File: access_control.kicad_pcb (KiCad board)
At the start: 2 copper layers, 72 parts, among them J1 Conn_01x04_Pin, J10 Screw_Terminal_01x02, J2 Screw_Terminal_01x04, J3 Screw_Terminal_01x04, J4 Screw_Terminal_01x02, J5 Screw_Terminal_01x04, J6 Screw_Terminal_01x04, J7 Screw_Terminal_01x02, J8 Screw_Terminal_01x02, J9 Screw_Terminal_01x02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

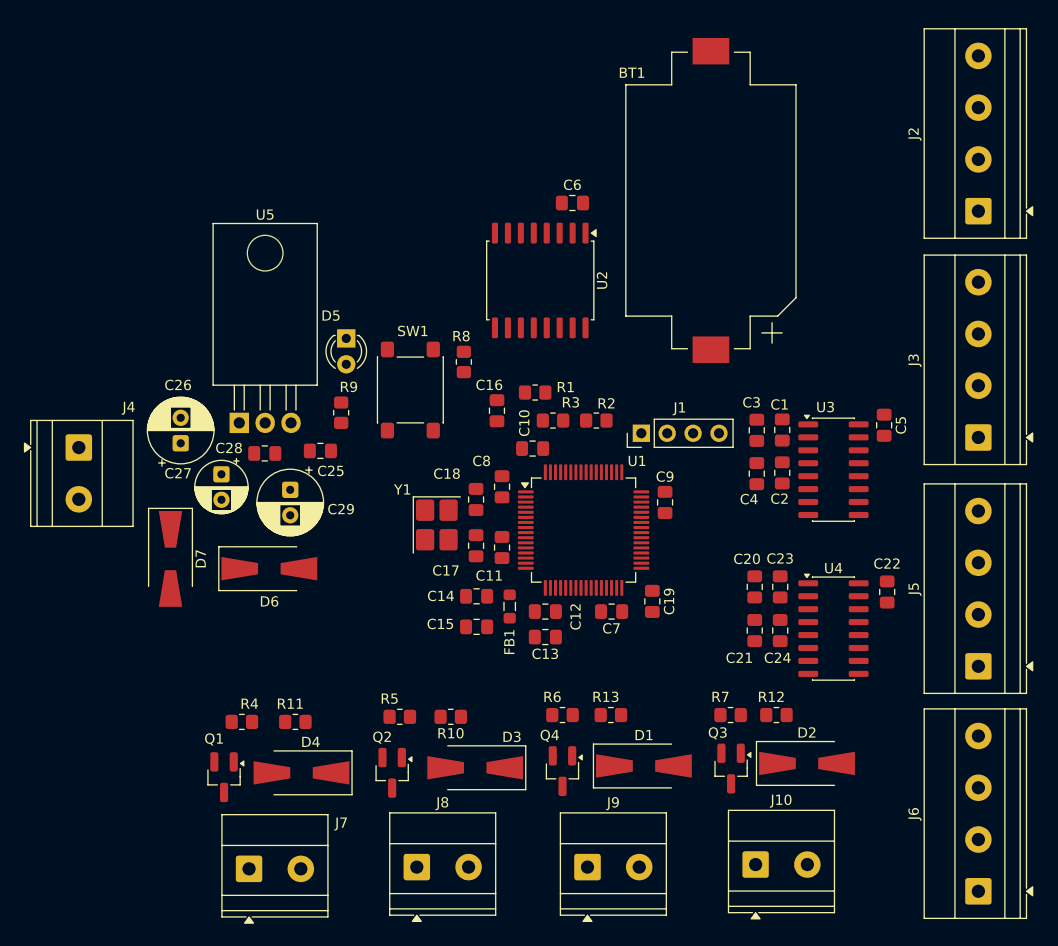
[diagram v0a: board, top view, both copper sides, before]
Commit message: Finished the PCB routing and placement of the components.
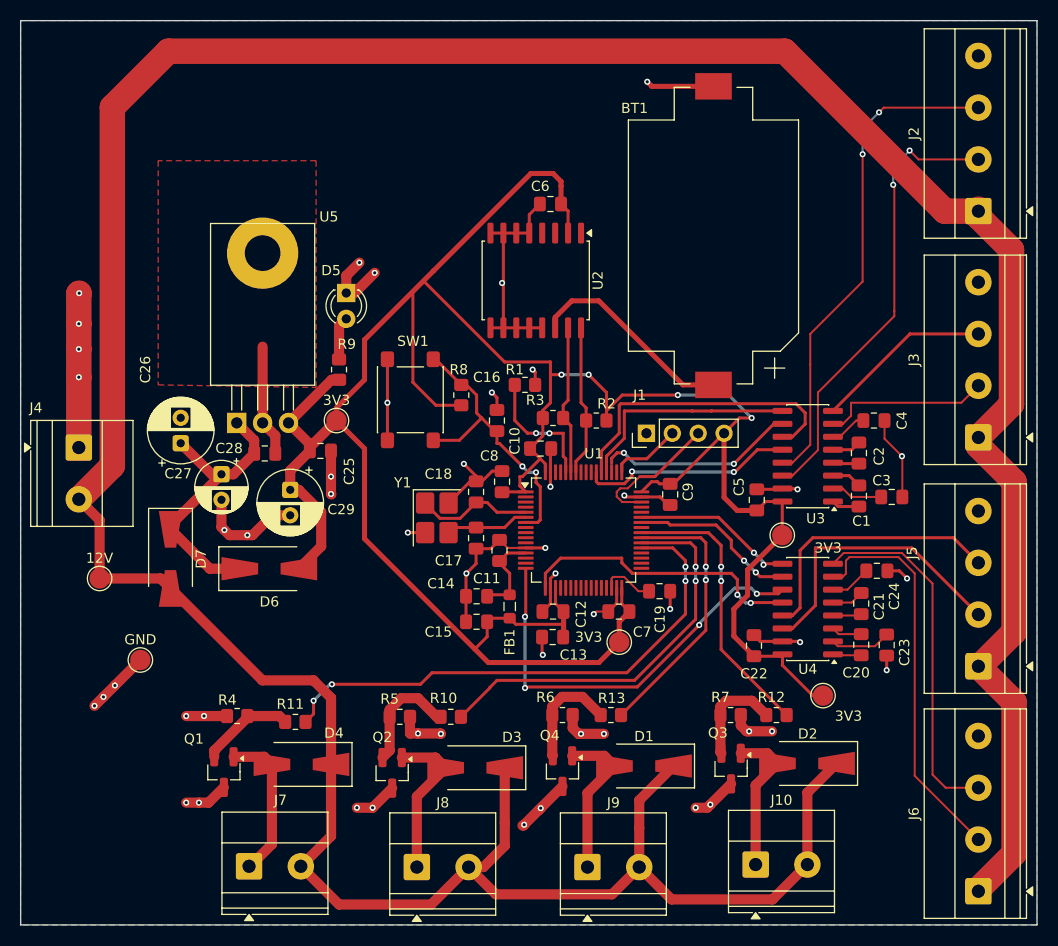
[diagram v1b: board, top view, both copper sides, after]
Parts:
- added 12V: TestPoint, TestPoint:TestPoint_Pad_D2.0mm, F.Cu at (70.5, 110.8)
- added 3V3: TestPoint, TestPoint:TestPoint_Pad_D2.0mm, F.Cu at (141.5, 122.2)
- added 3V3: TestPoint, TestPoint:TestPoint_Pad_D2.0mm, F.Cu at (121.5, 117.0)
- added 3V3: TestPoint, TestPoint:TestPoint_Pad_D2.0mm, F.Cu at (137.5, 106.5)
- added 3V3: TestPoint, TestPoint:TestPoint_Pad_D2.0mm, F.Cu at (93.8, 95.2)
- added GND: TestPoint, TestPoint:TestPoint_Pad_D2.0mm, F.Cu at (74.5, 118.8)
- moved C3 14.8 mm to (148.2, 102.8), turned to 0 degrees
- moved C5 14.5 mm to (135.0, 103.0), turned to 90 degrees
- moved C22 14.1 mm to (134.7, 117.3), turned to 90 degrees
- moved C4 12.6 mm to (146.5, 95.2), turned to 0 degrees
- moved C23 11.9 mm to (147.8, 117.3), turned to -90 degrees
- moved C20 11.9 mm to (145.2, 117.2), turned to 90 degrees
- moved C24 11.2 mm to (146.8, 110.0), turned to 0 degrees
- moved C21 10.8 mm to (145.2, 113.2), turned to 90 degrees
- moved C1 9.93 mm to (145.0, 102.7), turned to 90 degrees
- moved C2 7.77 mm to (145.0, 98.4), turned to 90 degrees
- moved D5 4.46 mm to (94.7, 82.7)
- moved R9 4.24 mm to (94.0, 90.2)
- moved BT1 3.46 mm to (130.8, 77.1)
- moved R8 3.26 mm to (106.0, 92.8)
- moved U4 3.17 mm to (140.0, 113.8), turned to 180 degrees
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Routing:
- net +12V: track 0.00 -> 355.3 mm
- net +3V3: track 0.00 -> 269.0 mm, vias 0 -> 4
- net GND: track 0.00 -> 197.7 mm, vias 0 -> 49
- net /DOOR1_GATE: track 0.00 -> 52.5 mm, vias 0 -> 4
- net /RS232_5_TX: track 0.00 -> 48.8 mm, vias 0 -> 2
- net /RS232_5_RX: track 0.00 -> 44.8 mm, vias 0 -> 2
- net /USART2_TX: track 0.00 -> 41.6 mm, vias 0 -> 4
- net /DOOR2_GATE: track 0.00 -> 39.6 mm, vias 0 -> 2
- net /RS232_1_RX: track 0.00 -> 38.9 mm
- net /RS232_1_TX: track 0.00 -> 35.2 mm
- net /UART5_TX: track 0.00 -> 29.8 mm
- net Net-(D6-K): track 0.00 -> 28.9 mm
- net /RS232_2_RX: track 0.00 -> 28.5 mm
- net /NRST: track 0.00 -> 28.4 mm, vias 0 -> 2
- net /USART2_RX: track 0.00 -> 28.3 mm, vias 0 -> 2
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- added copper zone on B.Cu, net GND
- added copper zone on F.Cu, net GND
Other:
- board outline added: 99.8 x 88.8 mm

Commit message: Finilized editing PCB, generated BOM and grb files. PCB files are sent to JLCPCB
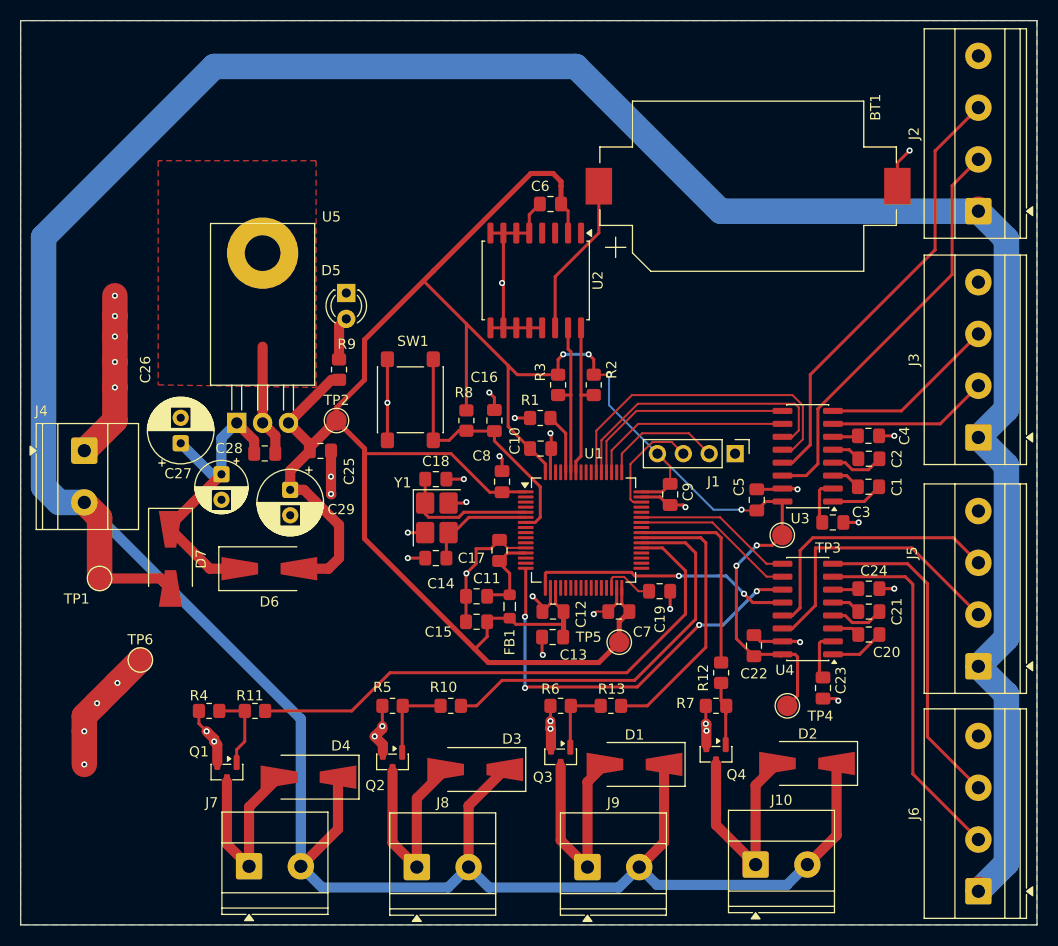
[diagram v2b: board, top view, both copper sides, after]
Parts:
- Q1, Q2, Q3, Q4: value NMOS -> FDV305N; footprint Package_TO_SOT_SMD:SOT-23_Handsoldering -> Package_TO_SOT_SMD:SOT-23
- moved Q3 16.8 mm to (115.8, 128.2)
- moved Q4 15.2 mm to (131.0, 128.0)
- moved J1 8.93 mm to (132.9, 98.5), turned to -90 degrees
- moved C23 7.54 mm to (141.5, 121.5)
- moved R12 6.84 mm to (131.5, 120.0), turned to -90 degrees
- moved C3 6.30 mm to (142.5, 105.2)
- moved BT1 5.92 mm to (134.2, 72.2), turned to 0 degrees
- moved C17 4.41 mm to (103.5, 108.8), turned to 180 degrees
- moved C18 4.14 mm to (103.5, 101.0), turned to 0 degrees
- moved R11 4.11 mm to (85.8, 123.8)
- moved TP4 3.64 mm to (138.0, 123.2)
- moved R1 3.58 mm to (113.8, 95.0), turned to 0 degrees
- moved R2 3.51 mm to (119.0, 91.8), turned to 90 degrees
- moved R3 3.29 mm to (115.5, 91.8), turned to 90 degrees
- moved R4 2.80 mm to (81.2, 123.8)
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- renumbered 12V to TP1, 3V3 to TP2, 3V3 to TP3, 3V3 to TP4, 3V3 to TP5, GND to TP6
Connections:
- Q1 pad 1: /DOOR1_DRAIN -> Net-(Q1-G)
- Q1 pad 2: Net-(Q1-G) -> GND
- Q1 pad 3: GND -> /DOOR1_DRAIN
- Q2 pad 1: /DOOR2_DRAIN -> Net-(Q2-G)
- Q2 pad 2: Net-(Q2-G) -> GND
- Q2 pad 3: GND -> /DOOR2_DRAIN
- Q3 pad 1: /DOOR4_DRAIN -> Net-(Q3-G)
- Q3 pad 2: Net-(Q3-G) -> GND
- Q3 pad 3: GND -> /DOOR3_DRAIN
- Q4 pad 1: /DOOR3_DRAIN -> Net-(Q4-G)
- Q4 pad 2: Net-(Q4-G) -> GND
- Q4 pad 3: GND -> /DOOR4_DRAIN
- R12 pad 2: Net-(Q3-G) -> Net-(Q4-G)
- R13 pad 2: Net-(Q4-G) -> Net-(Q3-G)
- R6 pad 2: Net-(Q4-G) -> Net-(Q3-G)
- R7 pad 2: Net-(Q3-G) -> Net-(Q4-G)
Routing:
- net GND: track 197.7 -> 157.3 mm, vias 49 -> 42
- net /UART5_RX: track 21.0 -> 32.0 mm, vias 2 -> 0
- net +12V: track 355.3 -> 365.9 mm
- net /DOOR4_DRAIN: track 14.8 -> 22.4 mm
- net /DOOR4_GATE: track 27.7 -> 20.3 mm, vias 2 -> 0
- net /BOOT0: track 12.7 -> 5.95 mm, vias 2 -> 0
- net /DOOR3_DRAIN: track 15.6 -> 22.1 mm
- net /DOOR2_DRAIN: track 15.6 -> 21.4 mm
- net /RS232_5_TX: track 48.8 -> 43.4 mm, vias 2 -> 0
- net Net-(Q4-G): track 10.7 -> 5.54 mm
- net /SWCLK: track 7.03 -> 12.1 mm
- net /DS3231_BAT: track 20.7 -> 15.7 mm
- net /RS232_5_RX: track 44.8 -> 40.4 mm, vias 2 -> 0
- net /DOOR1_DRAIN: track 15.1 -> 19.3 mm
- net +3V3: track 269.0 -> 264.8 mm, vias 4 -> 6
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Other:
- rule pad_to_mask_clearance: 0.05 -> 0
